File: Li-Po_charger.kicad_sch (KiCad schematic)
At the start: 36 parts, among them J1 Connector_USB_C, J2 BAT_18650_POS, J3 Output, J5 BAT_18650_NEG, Q1 FDN340P, Q2 AO3407, SW1 PWR, SW3 VOUT_SEL, U1 LN4056H, U2 TPS63802

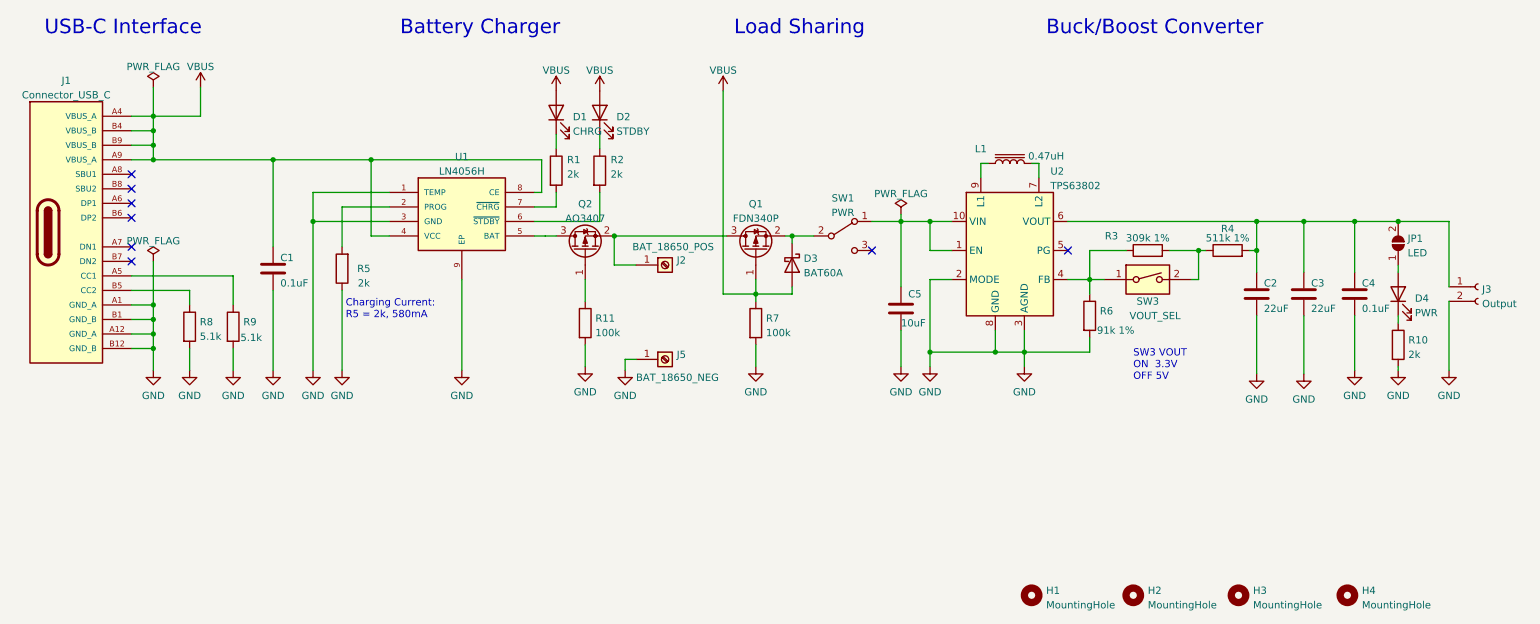
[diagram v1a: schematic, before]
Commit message: Add optional DW01A and latch interface to schematic
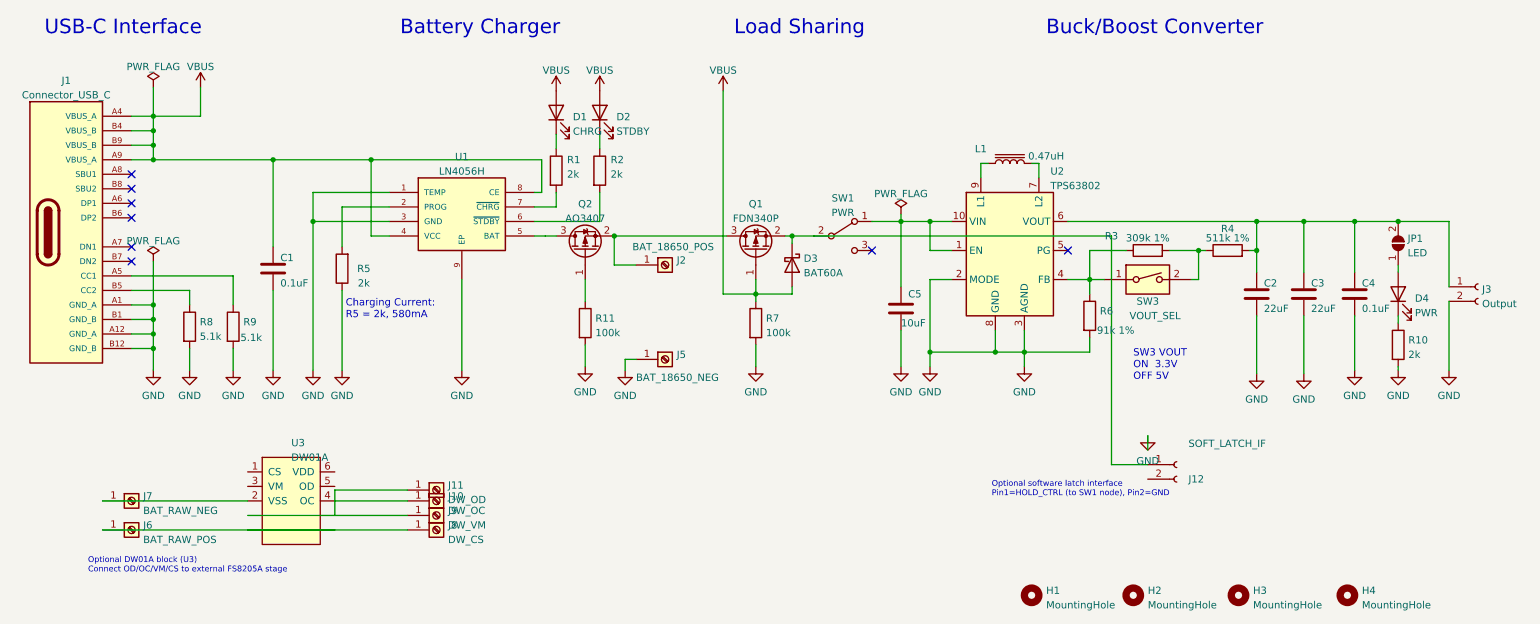
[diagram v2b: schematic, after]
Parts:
- added J10: DW_OC, Connector_Wire:SolderWirePad_1x01_Drill1mm, symbol Connector:Screw_Terminal_01x01
- added J11: DW_OD, Connector_Wire:SolderWirePad_1x01_Drill1mm, symbol Connector:Screw_Terminal_01x01
- added J12: SOFT_LATCH_IF, Connector_PinHeader_2.54mm:PinHeader_1x02_P2.54mm_Vertical, symbol Connector:Conn_01x02_Female
- added J6: BAT_RAW_POS, Connector_Wire:SolderWirePad_1x01_Drill1mm, symbol Connector:Screw_Terminal_01x01
- added J7: BAT_RAW_NEG, Connector_Wire:SolderWirePad_1x01_Drill1mm, symbol Connector:Screw_Terminal_01x01
- added J8: DW_CS, Connector_Wire:SolderWirePad_1x01_Drill1mm, symbol Connector:Screw_Terminal_01x01
- added J9: DW_VM, Connector_Wire:SolderWirePad_1x01_Drill1mm, symbol Connector:Screw_Terminal_01x01
- added U3: DW01A, Package_TO_SOT_SMD:SOT-23-6, symbol my_library:DW01A
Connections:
- net at D3.1 (K), Q1.2 (S), SW1.2 (B): now also J12.1 (Pin_1)
- new net: J6.1 (Pin_1), J8.1 (Pin_1)
- new net: J7.1 (Pin_1), U3.2 (VSS)
- new net: J10.1 (Pin_1), U3.4 (OC)
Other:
- note added: "Optional DW01A block (U3) Connect OD/OC/VM/CS to external FS8205A stage"
- note added: "Optional software latch interface Pin1=HOLD_CTRL (to SW1 node), Pin2=GND"
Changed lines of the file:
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@@
     )
+  )
+  (wire (pts (xy 33.02 148.59) (xy 73.66 148.59))
+    (stroke (width 0) (type default) (color 0 0 0 0))
+  )
+  (wire (pts (xy 33.02 143.51) (xy 58.42 143.51))
+    (stroke (width 0) (type default) (color 0 0 0 0))
+  )
+  (wire (pts (xy 58.42 148.59) (xy 86.36 148.59))
+    (stroke (width 0) (type default) (color 0 0 0 0))
+  )
+  (wire (pts (xy 58.42 146.05) (xy 86.36 146.05))
+    (stroke (width 0) (type default) (color 0 0 0 0))
+  )
+  (wire (pts (xy 73.66 143.51) (xy 86.36 143.51))
+    (stroke (width 0) (type default) (color 0 0 0 0))
+  )
+  (wire (pts (xy 73.66 146.05) (xy 73.66 141.605))
+    (stroke (width 0) (type default) (color 0 0 0 0))
+  )
+  (wire (pts (xy 73.66 141.605) (xy 86.36 141.605))
+    (stroke (width 0) (type default) (color 0 0 0 0))
+  )
+  (wire (pts (xy 157.48 97.155) (xy 209.55 97.155))
+    (stroke (width 0) (type default) (color 0 0 0 0))
+  )
+  (wire (pts (xy 209.55 97.155) (xy 209.55 137.16))
+    (stroke (width 0) (type default) (color 0 0 0 0))
+  )
+  (wire (pts (xy 209.55 137.16) (xy 215.9 137.16))
+    (stroke (width 0) (type default) (color 0 0 0 0))
+  )
+  (wire (pts (xy 215.9 134.62) (xy 215.9 132.08))
+    (stroke (width 0) (type default) (color 0 0 0 0))
+  )
+  (text "Optional DW01A block (U3)
+Connect OD/OC/VM/CS to external FS8205A stage" (at 30.48 156.21 0)
+    (effects (font (size 1.016 1.016)) (justify left bottom))
+  )
+  (text "Optional software latch interface
+Pin1=HOLD_CTRL (to SW1 node), Pin2=GND" (at 188.595 142.875 0)
+    (effects (font (size 1.016 1.016)) (justify left bottom))
+  )
+  (symbol (lib_id "Connector:Screw_Terminal_01x01") (at 38.1 148.59 0) (unit 1)
+    (in_bom yes) (on_board yes)
+    (property "Reference" "J6" (id 0) (at 40.132 147.7553 0)
+      (effects (font (size 1.27 1.27)) (justify left))
+    )
+    (property "Value" "BAT_RAW_POS" (id 1) (at 40.132 150.2922 0)
+      (effects (font (size 1.27 1.27)) (justify left))
+    )
+    (property "Footprint" "Connector_Wire:SolderWirePad_1x01_Drill1mm" (id 2) (at 38.1 148.59 0)
+      (effects (font (size 1.27 1.27)) hide)
+    )
+    (property "Datasheet" "~" (id 3) (at 38.1 148.59 0)
+      (effects (font (size 1.27 1.27)) hide)
+    )
+    (pin "1")
+  )
+  (symbol (lib_id "Connector:Screw_Terminal_01x01") (at 38.1 143.51 0) (unit 1)
+    (in_bom yes) (on_board yes)
+    (property "Reference" "J7" (id 0) (at 40.132 142.6753 0)
+      (effects (font (size 1.27 1.27)) (justify left))
+    )
+    (property "Value" "BAT_RAW_NEG" (id 1) (at 40.132 145.2122 0)
+      (effects (font (size 1.27 1.27)) (justify left))
+    )
+    (property "Footprint" "Connector_Wire:SolderWirePad_1x01_Drill1mm" (id 2) (at 38.1 143.51 0)
+      (effects (font (size 1.27 1.27)) hide)
+    )
+    (property "Datasheet" "~" (id 3) (at 38.1 143.51 0)
+      (effects (font (size 1.27 1.27)) hide)
+    )
+    (pin "1")
+  )
+  (symbol (lib_id "my_library:DW01A") (at 66.04 143.51 0) (unit 1)
+    (in_bom yes) (on_board yes)
+    (property "Reference" "U3" (id 0) (at 66.04 133.35 0)
+      (effects (font (size 1.27 1.27)) (justify left))
+    )
+    (property "Value" "DW01A" (id 1) (at 66.04 135.89 0)
+      (effects (font (size 1.27 1.27)) (justify left))
+    )
+    (property "Footprint" "Package_TO_SOT_SMD:SOT-23-6" (id 2) (at 66.04 143.51 0)
+      (effects (font (size 1.27 1.27)) hide)
+    )
+    (property "Datasheet" "https://www.tinytransistors.net/wp-content/uploads/datasheets/DW01A-DS-10.pdf" (id 3) (at 66.04 143.51 0)
+      (effects (font (size 1.27 1.27)) hide)
+    )
+    (pin "1")
+    (pin "2")
+    (pin "3")
+    (pin "4")
+    (pin "5")
+    (pin "6")
+  )
+  (symbol (lib_id "Connector:Screw_Terminal_01x01") (at 91.44 148.59 0) (unit 1)
+    (in_bom yes) (on_board yes)
+    (property "Reference" "J8" (id 0) (at 93.472 147.7553 0)
+      (effects (font (size 1.27 1.27)) (justify left))
+    )
+    (property "Value" "DW_CS" (id 1) (at 93.472 150.2922 0)
+      (effects (font (size 1.27 1.27)) (justify left))
+    )
+    (property "Footprint" "Connector_Wire:SolderWirePad_1x01_Drill1mm" (id 2) (at 91.44 148.59 0)
+      (effects (font (size 1.27 1.27)) hide)
+    )
+    (property "Datasheet" "~" (id 3) (at 91.44 148.59 0)
+      (effects (font (size 1.27 1.27)) hide)
+    )
+    (pin "1")
+  )
+  (symbol (lib_id "Connector:Screw_Terminal_01x01") (at 91.44 146.05 0) (unit 1)
+    (in_bom yes) (on_board yes)
+    (property "Reference" "J9" (id 0) (at 93.472 145.2153 0)
+      (effects (font (size 1.27 1.27)) (justify left))
+    )
+    (property "Value" "DW_VM" (id 1) (at 93.472 147.7522 0)
+      (effects (font (size 1.27 1.27)) (justify left))
+    )
+    (property "Footprint" "Connector_Wire:SolderWirePad_1x01_Drill1mm" (id 2) (at 91.44 146.05 0)
+      (effects (font (size 1.27 1.27)) hide)
+    )
+    (property "Datasheet" "~" (id 3) (at 91.44 146.05 0)
+      (effects (font (size 1.27 1.27)) hide)
+    )
+    (pin "1")
+  )
+  (symbol (lib_id "Connector:Screw_Terminal_01x01") (at 91.44 143.51 0) (unit 1)
+    (in_bom yes) (on_board yes)
+    (property "Reference" "J10" (id 0) (at 93.472 142.6753 0)
+      (effects (font (size 1.27 1.27)) (justify left))
+    )
+    (property "Value" "DW_OC" (id 1) (at 93.472 145.2122 0)
+      (effects (font (size 1.27 1.27)) (justify left))
+    )
+    (property "Footprint" "Connector_Wire:SolderWirePad_1x01_Drill1mm" (id 2) (at 91.44 143.51 0)
+      (effects (font (size 1.27 1.27)) hide)
+    )
+    (property "Datasheet" "~" (id 3) (at 91.44 143.51 0)
+      (effects (font (size 1.27 1.27)) hide)
+    )
+    (pin "1")
+  )
+  (symbol (lib_id "Connector:Screw_Terminal_01x01") (at 91.44 141.605 0) (unit 1)
+    (in_bom yes) (on_board yes)
+    (property "Reference" "J11" (id 0) (at 93.472 140.7703 0)
+      (effects (font (size 1.27 1.27)) (justify left))
+    )
+    (property "Value" "DW_OD" (id 1) (at 93.472 143.3072 0)
+      (effects (font (size 1.27 1.27)) (justify left))
+    )
+    (property "Footprint" "Connector_Wire:SolderWirePad_1x01_Drill1mm" (id 2) (at 91.44 141.605 0)
+      (effects (font (size 1.27 1.27)) hide)
+    )
+    (property "Datasheet" "~" (id 3) (at 91.44 141.605 0)
+      (effects (font (size 1.27 1.27)) hide)
+    )
+    (pin "1")
+  )
+  (symbol (lib_id "Connector:Conn_01x02_Female") (at 220.98 137.16 0) (unit 1)
+    (in_bom yes) (on_board yes)
+    (property "Reference" "J12" (id 0) (at 223.012 139.6978 0)
+      (effects (font (size 1.27 1.27)) (justify left))
+    )
+    (property "Value" "SOFT_LATCH_IF" (id 1) (at 223.012 133.4772 0)
+      (effects (font (size 1.27 1.27)) (justify left))
+    )
+    (property "Footprint" "Connector_PinHeader_2.54mm:PinHeader_1x02_P2.54mm_Vertical" (id 2) (at 220.98 137.16 0)
+      (effects (font (size 1.27 1.27)) hide)
+    )
+    (property "Datasheet" "~" (id 3) (at 220.98 137.16 0)
+      (effects (font (size 1.27 1.27)) hide)
+    )
+    (pin "1")
+    (pin "2")
+  )
+  (symbol (lib_id "power:GND") (at 215.9 132.08 0) (unit 1)
+    (in_bom yes) (on_board yes) (fields_autoplaced)
+    (property "Reference" "#PWR023" (id 0) (at 215.9 138.43 0)
+      (effects (font (size 1.27 1.27)) hide)
+    )
+    (property "Value" "GND" (id 1) (at 215.9 136.5234 0))
+    (property "Footprint" "" (id 2) (at 215.9 132.08 0)
+      (effects (font (size 1.27 1.27)) hide)
+    )
+    (property "Datasheet" "" (id 3) (at 215.9 132.08 0)
+      (effects (font (size 1.27 1.27)) hide)
+    )
+    (pin "1")
   )
   (sheet_instances
@@
       (reference "U1") (unit 1) (value "LN4056H") (footprint "my_library:SOP127P600X175-9N")
     )
+    (path "/4de06428-c730-47ad-9935-25e3e3bf7aff"
+      (reference "J6") (unit 1) (value "BAT_RAW_POS") (footprint "Connector_Wire:SolderWirePad_1x01_Drill1mm")
+    )
+    (path "/4b2ec4e0-f061-418d-a994-a27d9ae6366e"
+      (reference "J7") (unit 1) (value "BAT_RAW_NEG") (footprint "Connector_Wire:SolderWirePad_1x01_Drill1mm")
+    )
+    (path "/2915fbd4-7b29-4cff-b4a6-93c75f9b83dc"
+      (reference "J8") (unit 1) (value "DW_CS") (footprint "Connector_Wire:SolderWirePad_1x01_Drill1mm")
+    )
+    (path "/5a0816e5-95d0-4011-985a-5d186580351d"
+      (reference "J9") (unit 1) (value "DW_VM") (footprint "Connector_Wire:SolderWirePad_1x01_Drill1mm")
+    )
+    (path "/bf590497-f0dd-4ac7-a465-74567c614c30"
+      (reference "J10") (unit 1) (value "DW_OC") (footprint "Connector_Wire:SolderWirePad_1x01_Drill1mm")
+    )
+    (path "/8eaba070-dcfe-4013-bdd2-5d3e2afbf383"
+      (reference "J11") (unit 1) (value "DW_OD") (footprint "Connector_Wire:SolderWirePad_1x01_Drill1mm")
+    )
+    (path "/a36cb71d-0921-497f-8210-e0c60fedb4d7"
+      (reference "J12") (unit 1) (value "SOFT_LATCH_IF") (footprint "Connector_PinHeader_2.54mm:PinHeader_1x02_P2.54mm_Vertical")
+    )
+    (path "/062f95be-ecfb-49a0-80e2-a7e823259a0f"
+      (reference "#PWR023") (unit 1) (value "GND") (footprint "")
+    )
+    (path "/da0357d8-11b6-4536-be0a-ca240359bd73"
+      (reference "U3") (unit 1) (value "DW01A") (footprint "Package_TO_SOT_SMD:SOT-23-6")
+    )
     (path "/8858d596-b1d3-4897-8279-3e1676236e06"
